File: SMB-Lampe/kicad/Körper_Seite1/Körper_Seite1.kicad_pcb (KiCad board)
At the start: 2 copper layers, 121.9 x 96.3 mm, 32 parts, among them J1 Conn_01x01_Pin, J2 Conn_01x01_Pin, J3 Conn_01x01_Pin

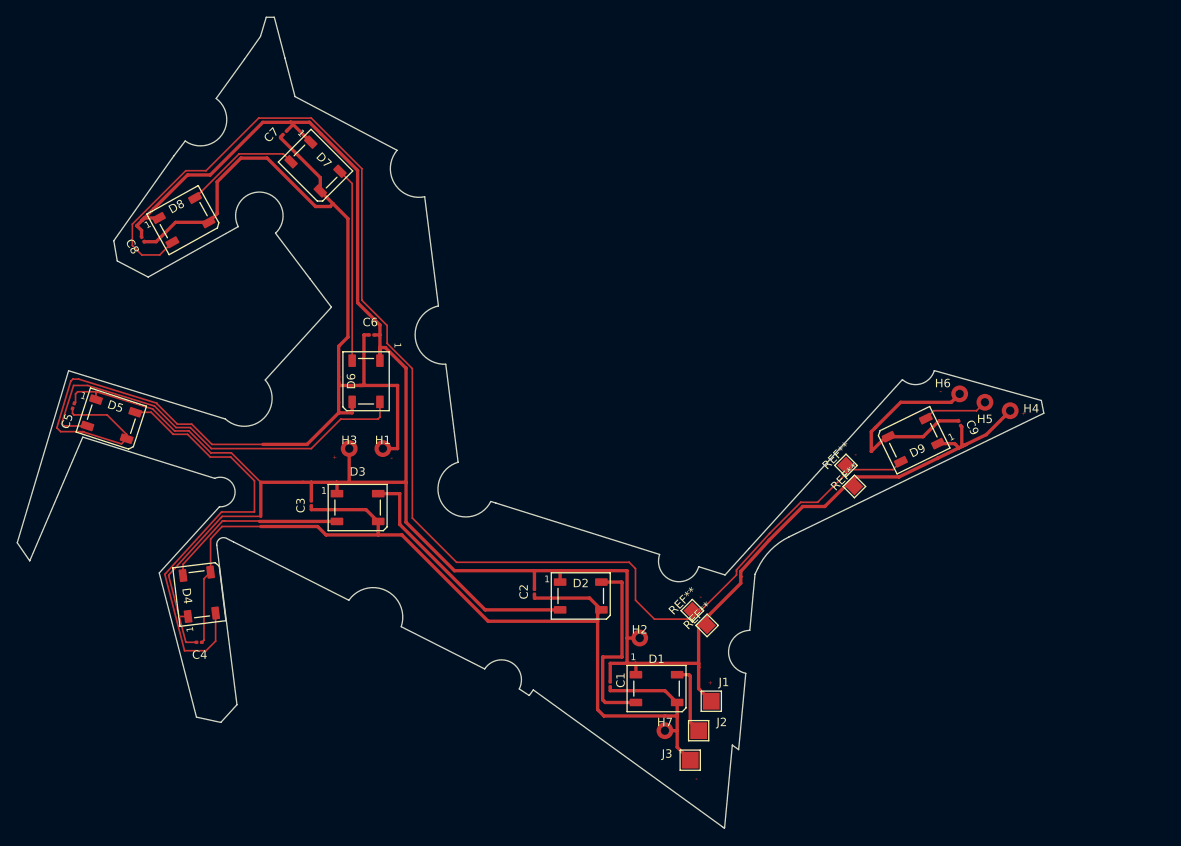
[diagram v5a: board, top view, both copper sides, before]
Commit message: Hinterbeine Geändert teilweiße Körper
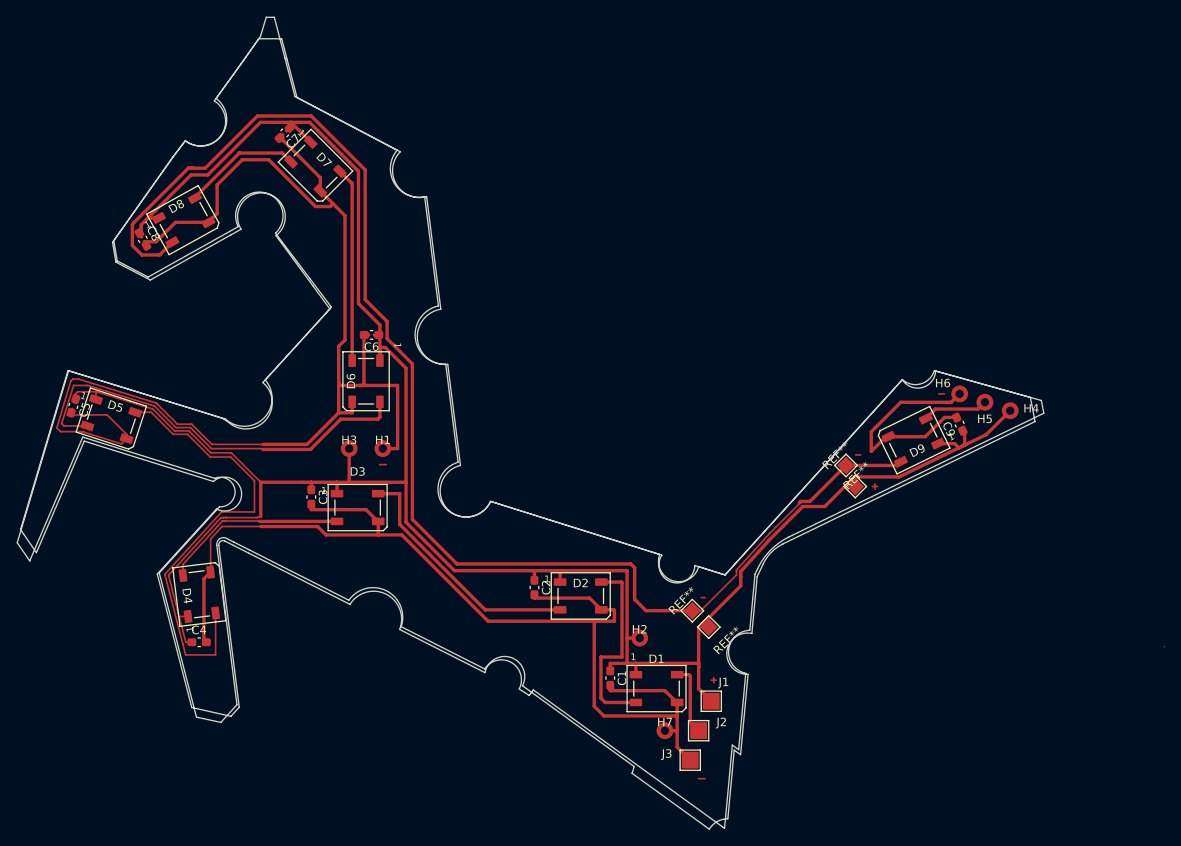
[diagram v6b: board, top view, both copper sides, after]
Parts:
- C1, C2, C3, C4, C5, C6, C7, C8, C9: footprint Capacitor_SMD:C_0201_0603Metric -> Capacitor_SMD:C_0603_1608Metric_Pad1.08x0.95mm_HandSolder
- moved C1 0.75 mm to (141.5, 132.8)
- moved C3 0.75 mm to (106.0, 111.2)
- moved C2 0.50 mm to (132.5, 122.0)
- moved REF** 0.28 mm to (153.2, 126.7)
- moved C9 0.10 mm to (183.0, 102.6)
- moved REF** 0.10 mm to (170.6, 110.0)
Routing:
- net (no net): track 0.00 -> 5.75 mm
- net +5V: track 293.8 -> 288.8 mm
- net GND: track 303.9 -> 308.0 mm
- net Net-(D4-DOUT): track 52.0 -> 53.6 mm
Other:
- board size 121.9 x 96.3 mm -> 136.3 x 96.4 mm
- board text removed: "+"
- board text removed: "-"

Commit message: Alle Platinen sind fertig zur Fertigung
Aus diesem Stand folgt das erste fertig leuchtende Pferd
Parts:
- moved C5 0.15 mm to (77.9, 100.4)
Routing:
- net GND: track 308.0 -> 304.4 mm
- net (no net): track 5.75 -> 8.65 mm
- net +5V: track 288.8 -> 286.1 mm
- net Net-(D4-DOUT): track 53.6 -> 54.1 mm
- net Net-(D8-DOUT): track 161.1 -> 161.7 mm
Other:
- board size 136.3 x 96.4 mm -> 378.4 x 106.1 mm

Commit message: Nachträgliche Änderungen für die Fertigung und Präsentation
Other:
- board size 378.4 x 106.1 mm -> 135.9 x 93.9 mm
